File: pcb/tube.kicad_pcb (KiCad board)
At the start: 2 copper layers, 99.1 x 116.8 mm, 82 parts, among them J1 Screw_Terminal_01x02, J10 LED_[5..8], J11 LED_[1..4], J2 Screw_Terminal_01x02, J3 Screw_Terminal_01x02, J4 Conn_01x04_Pin, J5 Conn_01x10_Pin, J6 Conn_01x05_Pin, U1 INA226, U10 74LS32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

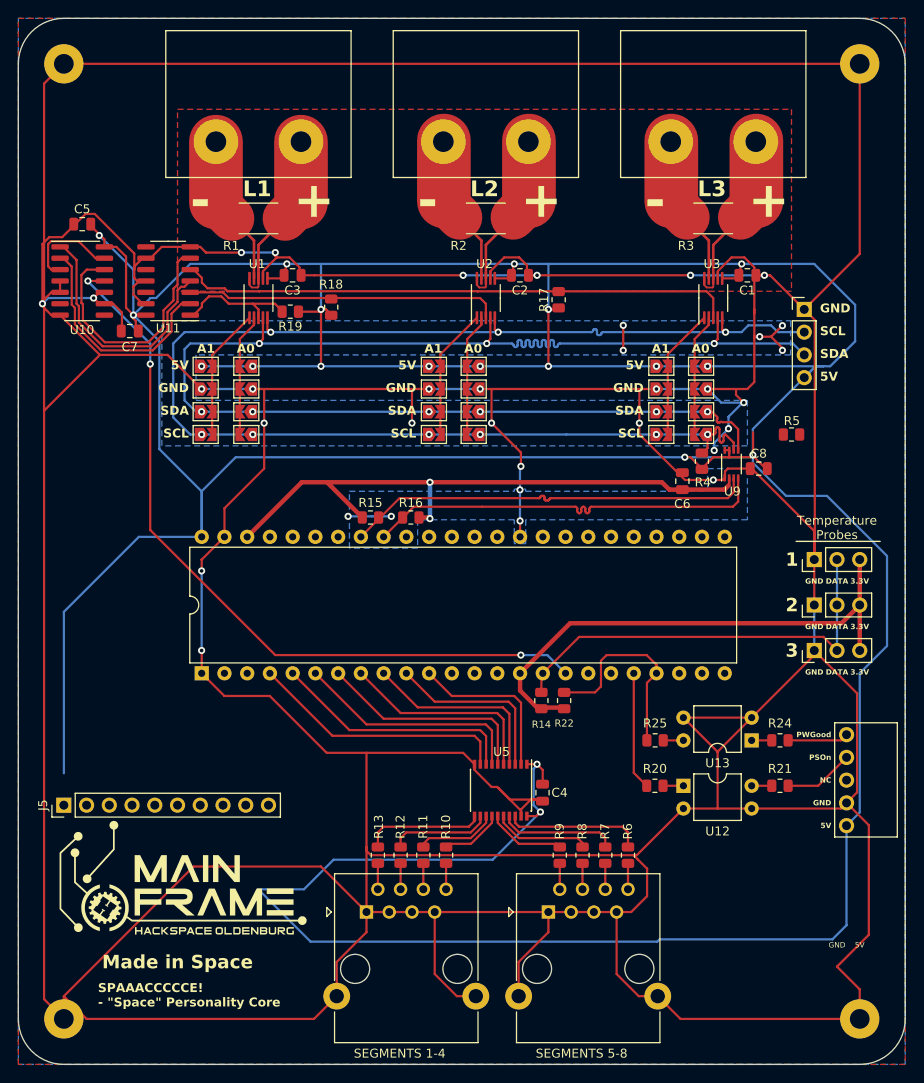
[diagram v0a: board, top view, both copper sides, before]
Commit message: PCB: Add SPI Voltage Shift
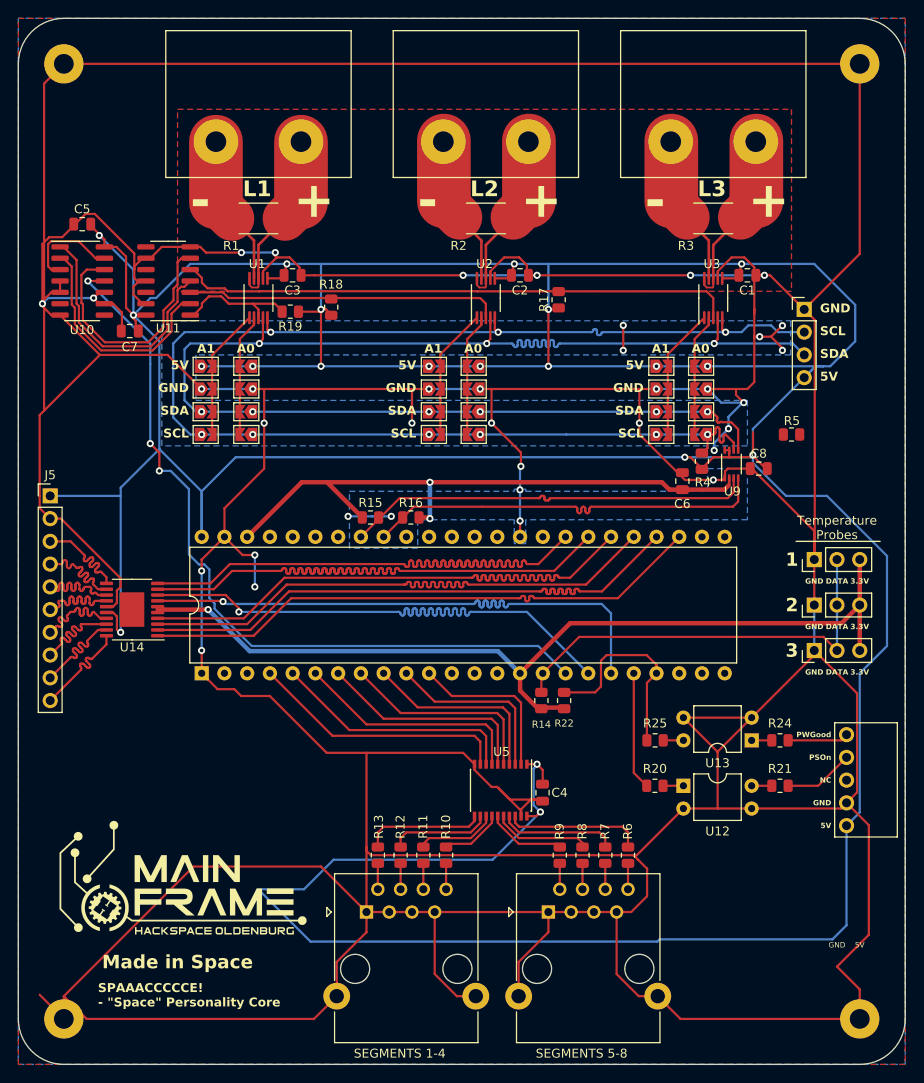
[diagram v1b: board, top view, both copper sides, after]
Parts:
- added U14: TXB0108DQSR, Package_SO:HTSSOP-20-1EP_4.4x6.5mm_P0.65mm_EP2.74x3.86mm, F.Cu at (154.9, 170.2)
- moved J5 34.6 mm to (145.8, 157.5), turned to 0 degrees
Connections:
- U4 pad 26: /CS5 -> unconnected-(U4-34_RX8-Pad26)
- U4 pad 27: /CS4 -> /CS1
- U4 pad 28: /CS3 -> /CS2
- U4 pad 29: /CS2 -> /CS3
- U4 pad 30: /CS1 -> /CS4
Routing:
- net /CS1: track 0.00 -> 64.0 mm
- net /CS2: track 0.00 -> 63.9 mm
- net /CS3: track 0.00 -> 63.8 mm
- net /CS4: track 0.00 -> 63.7 mm
- net /MISO: track 0.00 -> 63.6 mm
- net /RST: track 0.00 -> 63.6 mm
- net /SCK: track 0.00 -> 62.3 mm, vias 0 -> 1
- net /MOSI: track 0.00 -> 62.2 mm, vias 0 -> 1
- net /+3.3V1: track 59.3 -> 103.4 mm, vias 0 -> 1
- net GND: track 1026.2 -> 996.6 mm, vias 34 -> 36
- net Net-(J5-Pin_10): track 0.00 -> 11.9 mm
- net Net-(J5-Pin_3): track 0.00 -> 11.9 mm
- net Net-(J5-Pin_9): track 0.00 -> 11.9 mm
- net Net-(J5-Pin_8): track 0.00 -> 11.9 mm
- net Net-(J5-Pin_7): track 0.00 -> 11.9 mm
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
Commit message: PCB: Optimize Traces
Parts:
- moved J5 22.9 mm to (145.9, 180.3), turned to 180 degrees
- moved R5 4.85 mm to (223.8, 150.1)
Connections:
- J5 pad 1: +5V -> Net-(J5-Pin_1)
- J5 pad 10: Net-(J5-Pin_10) -> +5V
- J5 pad 2: GND -> Net-(J5-Pin_2)
- J5 pad 9: Net-(J5-Pin_9) -> GND
- U14 pad 11: Net-(J5-Pin_3) -> Net-(J5-Pin_8)
- U14 pad 12: Net-(J5-Pin_4) -> Net-(J5-Pin_7)
- U14 pad 13: Net-(J5-Pin_5) -> Net-(J5-Pin_6)
- U14 pad 14: Net-(J5-Pin_6) -> Net-(J5-Pin_5)
- U14 pad 17: Net-(J5-Pin_7) -> Net-(J5-Pin_4)
- U14 pad 18: Net-(J5-Pin_8) -> Net-(J5-Pin_3)
- U14 pad 19: Net-(J5-Pin_9) -> Net-(J5-Pin_2)
- U14 pad 20: Net-(J5-Pin_10) -> Net-(J5-Pin_1)
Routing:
- net Net-(J5-Pin_10): track 11.9 -> 0.00 mm
- net Net-(J5-Pin_1): track 0.00 -> 11.9 mm
- net Net-(J5-Pin_9): track 11.9 -> 0.00 mm
- net Net-(J5-Pin_2): track 0.00 -> 11.9 mm
- net GND: track 996.6 -> 989.1 mm, vias 36 -> 43
- net +5V: track 567.9 -> 561.8 mm
- net Net-(U4-25_A11_RX6_SDA2): track 87.6 -> 88.8 mm
